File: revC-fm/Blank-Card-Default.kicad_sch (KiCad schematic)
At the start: 40 parts, among them J1 ZX62-AB-5PA(31), Q11 BC847BM3T5G, Q12 BC847BM3T5G, Q13 BC847BM3T5G, Q14 BC847BM3T5G, SW2 SW_Push_SPST, U15 AP2161W

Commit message: working revC
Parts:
- renumbered C57 to C39, C58 to C40, C55 to C41, C56 to C42, C53 to C43, C54 to C44, C49 to C45, C50 to C46, C51 to C47, C52 to C48, D2 to D5, D3 to D6, D4 to D7, D5 to D8, Q11 to Q12, Q12 to Q13, Q13 to Q14, Q14 to Q15, R102 to R66, R99 to R67, R93 to R68, R96 to R69, R98 to R70, R101 to R71, R104 to R72, R92 to R73, R97 to R74, R100 to R75, R103 to R76, R95 to R77, R94 to R78, U15 to U9

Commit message: working revC
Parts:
- D13: renamed from D5; footprint SLI-Blank-Card:APA2107x -> SierraLobo:APA2107x; symbol mainboard-rescue:D-Device-mainboard-rescue -> Device:D
- D14: renamed from D6; footprint SLI-Blank-Card:APA2107x -> SierraLobo:APA2107x; symbol mainboard-rescue:D-Device-mainboard-rescue -> Device:D
- D15: renamed from D7; footprint SLI-Blank-Card:APA2107x -> SierraLobo:APA2107x; symbol mainboard-rescue:D-Device-mainboard-rescue -> Device:D
- D16: renamed from D8; footprint SLI-Blank-Card:APA2107x -> SierraLobo:APA2107x; symbol mainboard-rescue:D-Device-mainboard-rescue -> Device:D
- H1: footprint SLI-Backplane-Blank-Card-KiCad:125mil_hole -> SierraLobo:125mil_hole; symbol mainboard-rescue:MountingHole_Pad-Mechanical-mainboard-rescue -> Mechanical:MountingHole_Pad; now left out of the parts list
- H2, H3, H4: value SLI-Backplane-Blank-Card-KiCad:125mil_hole -> MountingHole_Pad; footprint SLI-Backplane-Blank-Card-KiCad:125mil_hole -> SierraLobo:125mil_hole; symbol mainboard-rescue:MountingHole_Pad-Mechanical-mainboard-rescue -> Mechanical:MountingHole_Pad; now left out of the parts list
- J9: renamed from J1; footprint SLI-Backplane-Blank-Card-KiCad:ZX62-AB-5PA(31) -> SierraLobo:ZX62-AB-5PA(31); symbol mainboard-rescue:USB_B_Micro-Connector-mainboard-rescue -> Connector:USB_B_Micro
- Q42: renamed from Q12; symbol mainboard-rescue:Q_NPN_BEC-Device-mainboard-rescue -> Device:Q_NPN_BEC
- Q43: renamed from Q13; symbol mainboard-rescue:Q_NPN_BEC-Device-mainboard-rescue -> Device:Q_NPN_BEC
- Q44: renamed from Q14; symbol mainboard-rescue:Q_NPN_BEC-Device-mainboard-rescue -> Device:Q_NPN_BEC
- Q45: renamed from Q15; symbol mainboard-rescue:Q_NPN_BEC-Device-mainboard-rescue -> Device:Q_NPN_BEC
- R209: renamed from R77; value DNP -> 0; now not fitted
- SW3: renamed from SW2; footprint SLI-Blank-Card:EVQP7C01P -> SierraLobo:EVQP7C01P
- U23: renamed from U9; symbol mainboard-rescue:AP2161W-Power_Management-mainboard-rescue -> Power_Management:AP2161W
- Z1, Z2: symbol mainboard-rescue:Varistor-Device-mainboard-rescue -> Device:Varistor
- renumbered C39 to C86, C40 to C87, C41 to C88, C42 to C89, C43 to C90, C44 to C91, C45 to C92, C46 to C93, C47 to C94, C48 to C95, R66 to R198, R67 to R199, R68 to R200, R69 to R201, R70 to R202, R71 to R203, R72 to R204, R73 to R205, R74 to R206, R75 to R207, R76 to R208, R78 to R210
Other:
- note added: "U9 limits USB current to 1.5A (1A rec by mfr.)"
- note removed: "U200 limits USB current to 1.5A (1A rec by mfr.)"

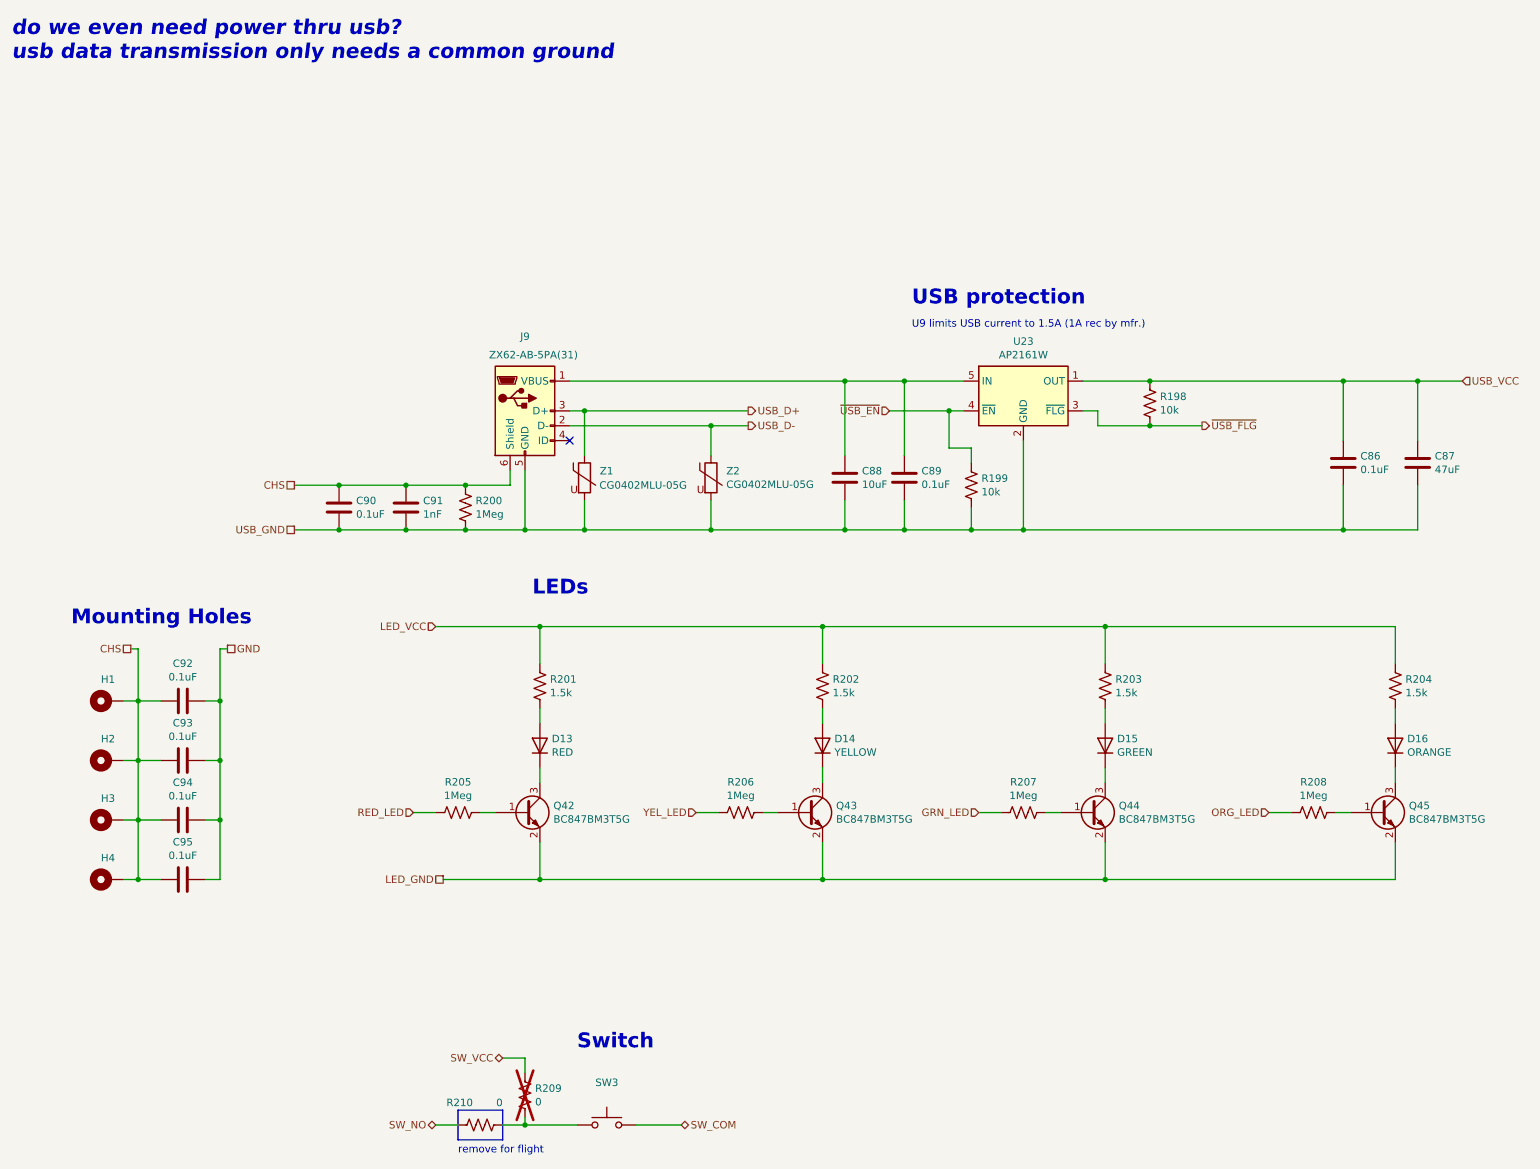
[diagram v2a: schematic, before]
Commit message: updated analog , solar comp, layout
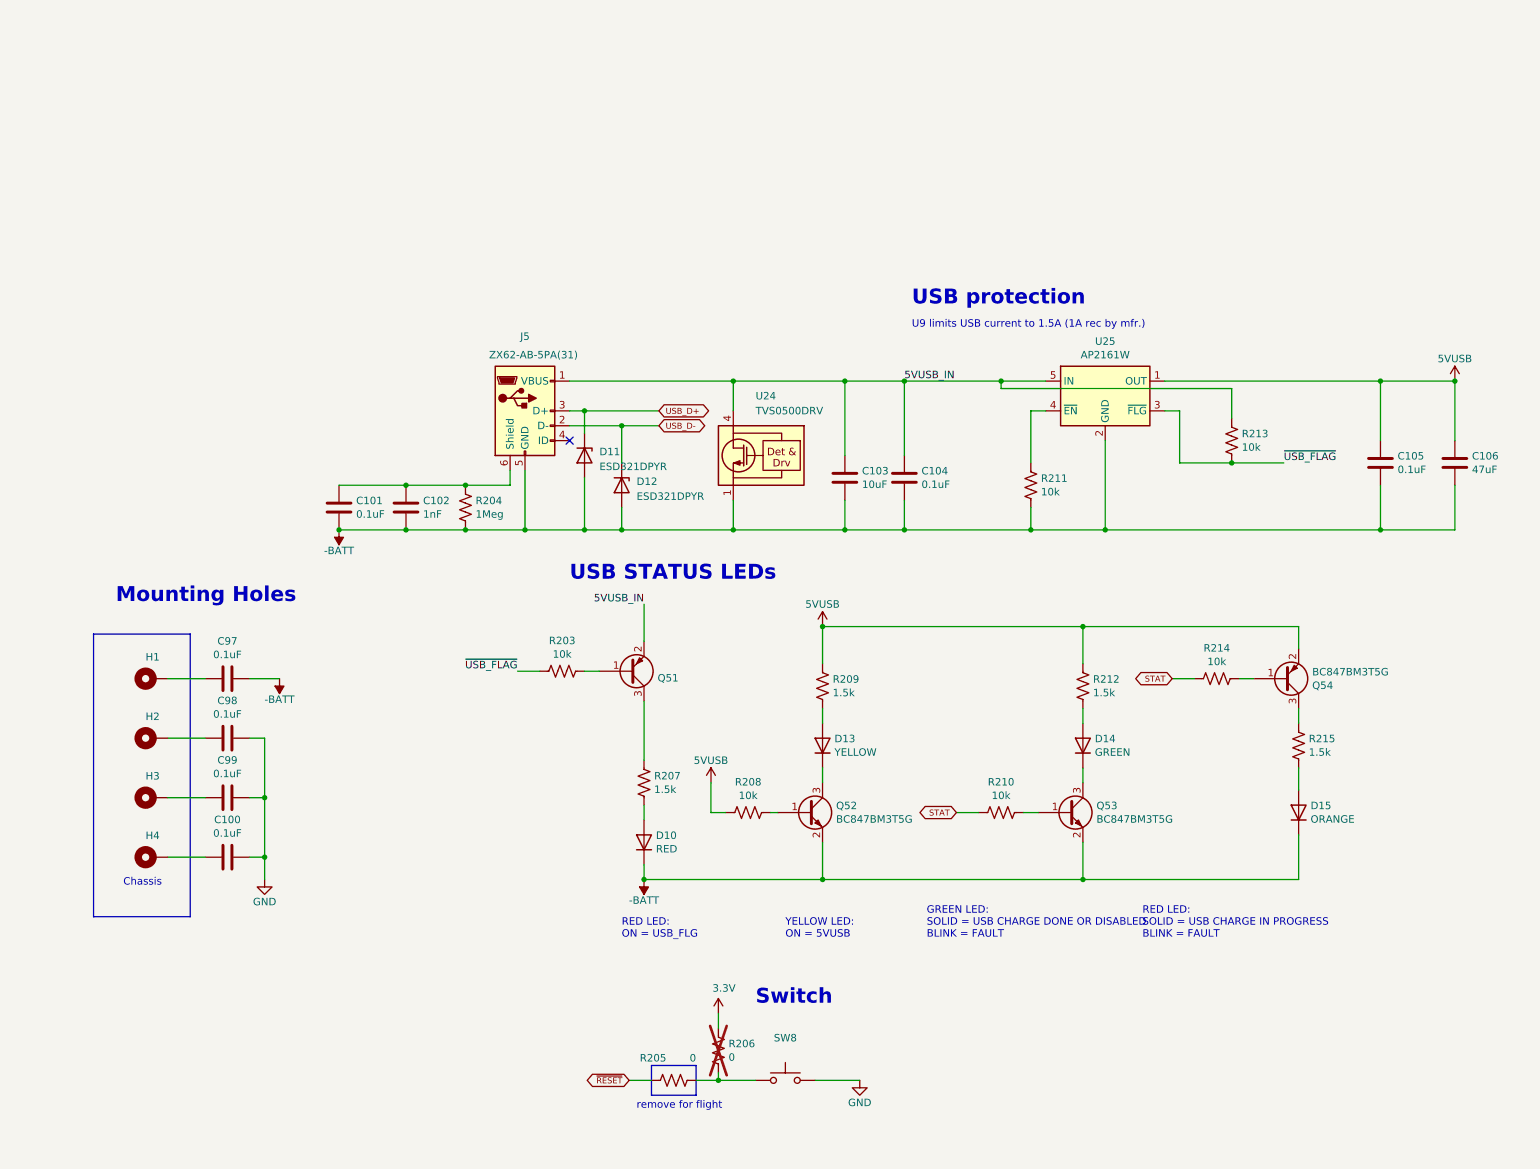
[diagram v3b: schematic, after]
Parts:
- removed Z1, Z2: CG0402MLU-05G, Capacitor_SMD:C_0402_1005Metric, symbol Device:Varistor
- added D11, D12: ESD321DPYR, Diode_SMD:D_0402_1005Metric, symbol Device:D_Zener
- added U24: TVS0500DRV, Package_SON:WSON-6-1EP_2x2mm_P0.65mm_EP1x1.6mm, symbol Power_Protection:TVS0500DRV
- Q51: renamed from Q42; value BC847BM3T5G -> ~; symbol Device:Q_NPN_BEC -> Device:Q_PNP_BEC
- Q54: renamed from Q45; symbol Device:Q_NPN_BEC -> Device:Q_PNP_BEC
- R203: renamed from R205; value 1Meg -> 10k
- R208: renamed from R206; value 1Meg -> 10k
- R210: renamed from R207; value 1Meg -> 10k
- R214: renamed from R208; value 1Meg -> 10k
- renumbered C95 to C100, C90 to C101, C91 to C102, C88 to C103, C89 to C104, C86 to C105, C87 to C106, C92 to C97, C93 to C98, C94 to C99, D13 to D10, D14 to D13, D15 to D14, D16 to D15, J9 to J5, Q43 to Q52, Q44 to Q53, R200 to R204, R210 to R205, R209 to R206, R201 to R207, R202 to R209, R199 to R211, R203 to R212, R198 to R213, R204 to R215, SW3 to SW8, U23 to U25
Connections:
- net ORG_LED is gone; now on net STAT: R214.2
- net SW_COM is gone; now on net GND: SW8.2
- net USB_GND is gone; now on net -BATT: C101.2, C102.2, C103.2, C104.2, C105.2, C106.2, J5.5 (GND), R204.2, R211.2, U25.2 (GND)
- net YEL_LED is gone; now on net +5V: R208.2
- net ~{USB_FLG} is gone; now on net ~{USB_FLAG}: R213.2, U25.3 (~{FLG})
- net GND: no longer C97.1
- net USB_D+: now also D11.1 (K)
- net USB_D-: now also D12.1 (K)
- net 5VUSB_IN: now reaches C103.1, C104.1, J5.1 (VBUS), U25.5 (IN)
- net 5VUSB_IN: now also Q51.2 (E), R213.1, U24.4 (IN), U24.5 (IN), U24.6 (IN)
- net at Q51.3 (C): now also R207.1; no longer D10.1 (K)
- net at Q54.3 (C): now also R215.1; no longer D15.1 (K)
- removed net CHS: C100.2, C101.1, C102.1, C97.2, C98.2, C99.2, H1.1, H2.1, H3.1, H4.1, J5.6 (Shield), R204.1
- net GRN_LED renamed STAT
- net LED_GND renamed -BATT
- net -BATT: now also C97.1, D10.1 (K), D15.1 (K), D11.2 (A), D12.2 (A), U24.1 (GND), U24.2 (GND), U24.3 (GND), U24.7 (GND); no longer Q51.2 (E), Q54.2 (E)
- net LED_VCC renamed +5V
- net +5V: now also C105.1, C106.1, Q54.2 (E), U25.1 (OUT); no longer R207.1, R215.1
- net RED_LED renamed ~{USB_FLAG}
- net SW_NO renamed ~{RESET}
- net SW_VCC renamed 3.3V
- removed net USB_VCC: C105.1, C106.1, R213.1, U25.1 (OUT)
- net ~{USB_EN}: no longer names the net of R211.1, U25.4 (~{EN})
- new net: C101.1, C102.1, J5.6 (Shield), R204.1
- new net: C97.2, H1.1
- new net: C98.2, H2.1
- new net: C99.2, H3.1
- new net: C100.2, H4.1
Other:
- note added: "Chassis"
- note added: "GREEN LED: SOLID = USB CHARGE DONE OR DISABLED BLINK = FAULT"
- note added: "RED LED: ON = USB_FLG"
- note added: "RED LED: SOLID = USB CHARGE IN PROGRESS BLINK = FAULT"
- note added: "USB STATUS LEDs"
- note added: "YELLOW LED: ON = 5VUSB"
- note removed: "LEDs"
- note removed: "do we even need power thru usb? usb data transmission only needs a common ground"
- moved on the sheet: C100, C105, C106, C97, C98, C99, D10, D14, D15, H1, H2, H3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

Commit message: routing
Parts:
- C117: renamed from C97; footprint Capacitor_SMD:C_0402_1005Metric -> Capacitor_SMD:C_0603_1608Metric
- C118: renamed from C98; footprint Capacitor_SMD:C_0402_1005Metric -> Capacitor_SMD:C_0603_1608Metric
- C119: renamed from C99; footprint Capacitor_SMD:C_0402_1005Metric -> Capacitor_SMD:C_0603_1608Metric
- C120: renamed from C100; footprint Capacitor_SMD:C_0402_1005Metric -> Capacitor_SMD:C_0603_1608Metric
- renumbered C105 to C111, C106 to C112, C103 to C113, C104 to C114, C101 to C115, C102 to C116, D11 to D10, D12 to D11, D13 to D12, D14 to D13, D15 to D14, D10 to D15, Q51 to Q52, Q54 to Q53, Q52 to Q54, Q53 to Q55, R213 to R196, R211 to R197, R204 to R198, R203 to R199, R214 to R200, R209 to R201, R212 to R202, R215 to R203, R207 to R204, R208 to R205, R210 to R206, R206 to R207, R205 to R208, U25 to U27, U24 to U28
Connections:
- net +5V renamed 5VUSB

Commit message: fm layout
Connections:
- net -BATT: now also C118.1; no longer C117.1
- net GND: now also C117.1; no longer C118.1
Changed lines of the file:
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@@
   (junction (at 154.94 46.99) (diameter 0) (color 0 0 0 0)
-  )
-  (junction (at 55.88 118.11) (diameter 0) (color 0 0 0 0)
   )
   (junction (at 68.58 72.39) (diameter 0) (color 0 0 0 0)
@@
     (stroke (width 0) (type default))
   )
-  (wire (pts (xy 53.34 97.79) (xy 58.42 97.79))
+  (wire (pts (xy 53.34 97.79) (xy 57.15 97.79))
     (stroke (width 0) (type default))
   )
@@
   )
   (wire (pts (xy 195.58 88.9) (xy 195.58 95.25))
-    (stroke (width 0) (type default))
-  )
-  (wire (pts (xy 55.88 107.95) (xy 55.88 118.11))
     (stroke (width 0) (type default))
   )
@@
     )
   )
-  (symbol (lib_id "power:-BATT") (at 58.42 97.79 180) (unit 1)
-    (in_bom yes) (on_board yes) (dnp no)
-    (property "Reference" "#PWR020" (at 58.42 93.98 0)
-      (effects (font (size 1.27 1.27)) hide)
-    )
-    (property "Value" "-BATT" (at 58.42 101.346 0)
-      (effects (font (size 1.27 1.27)))
-    )
-    (property "Footprint" "" (at 58.42 97.79 0)
-      (effects (font (size 1.27 1.27)) hide)
-    )
-    (property "Datasheet" "" (at 58.42 97.79 0)
-      (effects (font (size 1.27 1.27)) hide)
-    )
-    (pin "1")
-    (instances
-      (project "mainboard"
-        (path "/d1441985-7b63-4bf8-a06d-c70da2e3b78b"
-          (reference "#PWR020") (unit 1)
-        )
-        (path "/d1441985-7b63-4bf8-a06d-c70da2e3b78b/81f44d01-bc9f-4b7f-b957-1cda63083cdb"
-          (reference "#PWR0152") (unit 1)
-        )
-      )
-    )
-  )
   (symbol (lib_id "power:-BATT") (at 68.58 72.39 180) (unit 1)
     (in_bom yes) (on_board yes) (dnp no)
@@
         )
       )
+    )
+  )
+  (symbol (lib_id "power:-BATT") (at 55.88 107.95 180) (unit 1)
+    (in_bom yes) (on_board yes) (dnp no)
+    (property "Reference" "#PWR020" (at 55.88 104.14 0)
+      (effects (font (size 1.27 1.27)) hide)
+    )
+    (property "Value" "-BATT" (at 55.88 111.506 0)
+      (effects (font (size 1.27 1.27)))
+    )
+    (property "Footprint" "" (at 55.88 107.95 0)
+      (effects (font (size 1.27 1.27)) hide)
+    )
+    (property "Datasheet" "" (at 55.88 107.95 0)
+      (effects (font (size 1.27 1.27)) hide)
+    )
+    (pin "1")
+    (instances
+      (project "mainboard"
+        (path "/d1441985-7b63-4bf8-a06d-c70da2e3b78b"
+          (reference "#PWR020") (unit 1)
+        )
+        (path "/d1441985-7b63-4bf8-a06d-c70da2e3b78b/81f44d01-bc9f-4b7f-b957-1cda63083cdb"
+          (reference "#PWR06") (unit 1)
+        )
+      )
+    )
+  )
+  (symbol (lib_id "power:GND") (at 57.15 97.79 0) (unit 1)
+    (in_bom yes) (on_board yes) (dnp no)
+    (property "Reference" "#PWR019" (at 57.15 104.14 0)
+      (effects (font (size 1.27 1.27)) hide)
+    )
+    (property "Value" "GND" (at 57.15 101.6 0)
+      (effects (font (size 1.27 1.27)))
+    )
+    (property "Footprint" "" (at 57.15 97.79 0)
+      (effects (font (size 1.27 1.27)) hide)
+    )
+    (property "Datasheet" "" (at 57.15 97.79 0)
+      (effects (font (size 1.27 1.27)) hide)
+    )
+    (pin "1")
+    (instances
+      (project "mainboard"
+        (path "/d1441985-7b63-4bf8-a06d-c70da2e3b78b"
+          (reference "#PWR019") (unit 1)
+        )
+        (path "/d1441985-7b63-4bf8-a06d-c70da2e3b78b/81f44d01-bc9f-4b7f-b957-1cda63083cdb"
+          (reference "#PWR069") (unit 1)
+        )
+      )

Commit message: changed RF connector to TH
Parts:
- D10, D11: footprint Diode_SMD:D_0402_1005Metric -> SierraLobo:D_0402_1005Metric
- Q51: renamed from Q52; footprint Package_TO_SOT_SMD:SOT-723 -> SierraLobo:SOT-723
- Q52: renamed from Q53; footprint Package_TO_SOT_SMD:SOT-723 -> SierraLobo:SOT-723
- Q53: renamed from Q54; footprint Package_TO_SOT_SMD:SOT-723 -> SierraLobo:SOT-723
- Q54: renamed from Q55; footprint Package_TO_SOT_SMD:SOT-723 -> SierraLobo:SOT-723
- renumbered C111 to C101, C112 to C102, C113 to C103, C114 to C104, C115 to C105, C116 to C106, C117 to C107, C118 to C108, C119 to C109, C120 to C110, R196 to R192, R197 to R193, R198 to R194, R199 to R195, R200 to R196, R201 to R197, R202 to R198, R203 to R199, R204 to R200, R205 to R201, R206 to R202, R207 to R203, R208 to R204, SW8 to SW9, U27 to U25, U28 to U26

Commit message: working revC review changes
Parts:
- renumbered C101 to C102, C102 to C103, C103 to C104, C104 to C105, C105 to C106, C106 to C107, C107 to C108, C108 to C109, C109 to C110, C110 to C111, D11 to D10, D12 to D11, D13 to D12, D14 to D13, D15 to D14, D10 to D9, Q51 to Q56, Q52 to Q57, Q53 to Q58, Q54 to Q59, R192 to R207, R193 to R208, R194 to R209, R195 to R210, R196 to R211, R197 to R212, R198 to R213, R199 to R214, R200 to R215, R201 to R216, R202 to R217, R203 to R218, R204 to R219, SW9 to SW8, U25 to U26, U26 to U27
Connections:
- net 5VUSB: no longer R216.2
- new net WDT_WDI: R216.2
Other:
- note added: "YELLOW LED: ON = WDT_WDI"
- note removed: "YELLOW LED: ON = 5VUSB"

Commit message: working revC
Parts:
- removed Q56: ~, SierraLobo:SOT-723, symbol Device:Q_PNP_BEC
- removed Q57: BC847BM3T5G, SierraLobo:SOT-723, symbol Device:Q_PNP_BEC
- removed Q58, Q59: BC847BM3T5G, SierraLobo:SOT-723, symbol Device:Q_NPN_BEC
- removed R210, R211, R216, R217: 10k, Resistor_SMD:R_0402_1005Metric, symbol Device:R_US
- added Q73 (x2): MUN5311DW1, Package_TO_SOT_SMD:SOT-363_SC-70-6, symbol SierraLobo:MUN5312DW1
- C87: renamed from C103; Mfr. Part No (none) -> C3216X5R1E476M160AC
- C88: renamed from C104; Mfr. Part No (none) -> CGA4J1X7S1E106K125AE
- C92: renamed from C108; footprint Capacitor_SMD:C_0603_1608Metric -> Capacitor_SMD:C_0402_1005Metric
- C93: renamed from C109; footprint Capacitor_SMD:C_0603_1608Metric -> Capacitor_SMD:C_0402_1005Metric
- C94: renamed from C110; footprint Capacitor_SMD:C_0603_1608Metric -> Capacitor_SMD:C_0402_1005Metric
- C95: renamed from C111; footprint Capacitor_SMD:C_0603_1608Metric -> Capacitor_SMD:C_0402_1005Metric
- D4: renamed from D11; Mfr. Part No (none) -> APA2107SYCK/J3-PRV
- D5: renamed from D12; Mfr. Part No (none) -> APA2107CGCK
- D6: renamed from D13; Mfr. Part No (none) -> APA2107SECK/J4-PRV
- D7: renamed from D14; Mfr. Part No (none) -> APA2107LSECK/J3-PRV
- R149: renamed from R218; value 0 -> DNP
- R150: renamed from R219; footprint Resistor_SMD:R_0402_1005Metric -> Resistor_SMD:R_0603_1608Metric
- SW4: renamed from SW8; value SW_Push_SPST -> EVQP7C01P; Mfr. Part No (none) -> EVQP7C01P
- U25: renamed from U26; Mfr. Part No (none) -> AP2161W
- U26: renamed from U27; Mfr. Part No (none) -> TVS0500DRV
- renumbered C102 to C86, C105 to C89, C106 to C90, C107 to C91, D9 to D2, D10 to D3, R207 to R138, R208 to R139, R209 to R140, R212 to R143, R213 to R144, R214 to R145, R215 to R146
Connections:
- net -BATT: now also Q73.1 (E2), Q73.1 (E2)
- net 5VUSB: now also Q73.4 (E1); no longer R143.1
- net 5VUSB_IN: now also Q73.4 (E1)
- net STAT: now also Q73.2 (B2), Q73.5 (B1)
- net WDT_WDI: now also Q73.2 (B2)
- net ~{USB_FLAG}: now also Q73.5 (B1)
- net at R146.1: now also Q73.3 (C1)
- net at D4.1 (K): now also Q73.6 (C2)
- net at D5.1 (K): now also Q73.6 (C2)
- net at R145.1: now also Q73.3 (C1)
- new net LED_PWR: R143.1
